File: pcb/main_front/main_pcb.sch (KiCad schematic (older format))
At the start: 31 parts, among them J1 AVR-ISP-6, J2 USB_C_Receptacle_USB2.0, Q1 Q_NMOS_DGS, SW1 RESET, SW2 BOOT, SW3 BL_STEP, U1 ATmega32-16PU, Y1 Crystal

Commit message: Begin revised PCB layout
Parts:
- removed D2: NUMLOCK, LED_THT:LED_D3.0mm_Clear, symbol Device:LED
- removed R9: 1.5k, Resistor_THT:R_Axial_DIN0204_L3.6mm_D1.6mm_P7.62mm_Horizontal, symbol Device:R
- added J3: Conn_01x16_Male, Connector_PinHeader_2.54mm:PinHeader_2x08_P2.54mm_Horizontal, symbol Connector:Conn_01x16_Male
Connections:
- net +5V: now also J3.16 (Pin_16)
- net GND: now also J3.15 (Pin_15)
- net LEDGND: now also J3.10 (Pin_10)
- net NUMLOCK: now also J3.11 (Pin_11)
- net col16: now also J3.9 (Pin_9)
- net col17: now also J3.8 (Pin_8)
- net col18: now also J3.7 (Pin_7)
- net col19: now also J3.6 (Pin_6)
- net row0: now also J3.5 (Pin_5)
- net row1: now also J3.4 (Pin_4)
- net row2: now also J3.3 (Pin_3)
- net row3: now also J3.2 (Pin_2)
- net row4: now also J3.1 (Pin_1)
- no-connect marks 3 -> 6
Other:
- moved on the sheet: D5, R10
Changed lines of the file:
@@
 encoding utf-8
 Sheet 1 2
-Title "QBoard - Front"
+Title "QBoard - Main"
 Date "2021-08-26"
 Rev "0"
@@
 L Device:LED D5
 U 1 1 6129195C
-P 7975 4350
-F 0 "D5" H 7968 4095 50  0000 C CNN
-F 1 "POWER" H 7968 4186 50  0000 C CNN
-F 2 "LED_THT:LED_D3.0mm_Clear" H 7975 4350 50  0001 C CNN
-F 3 "~" H 7975 4350 50  0001 C CNN
-	1    7975 4350
+P 7975 3825
+F 0 "D5" H 7968 3570 50  0000 C CNN
+F 1 "POWER" H 7968 3661 50  0000 C CNN
+F 2 "LED_THT:LED_D3.0mm_Clear" H 7975 3825 50  0001 C CNN
+F 3 "~" H 7975 3825 50  0001 C CNN
+	1    7975 3825
 	-1   0    0    1
 $EndComp
@@
 L Device:R R10
 U 1 1 612935EF
-P 8275 4350
-F 0 "R10" V 8175 4350 50  0000 C CNN
-F 1 "1.5k" V 8275 4350 50  0000 C CNN
-F 2 "Resistor_THT:R_Axial_DIN0204_L3.6mm_D1.6mm_P7.62mm_Horizontal" V 8205 4350 50  0001 C CNN
-F 3 "~" H 8275 4350 50  0001 C CNN
-	1    8275 4350
+P 8275 3825
+F 0 "R10" V 8175 3825 50  0000 C CNN
+F 1 "1.5k" V 8275 3825 50  0000 C CNN
+F 2 "Resistor_THT:R_Axial_DIN0204_L3.6mm_D1.6mm_P7.62mm_Horizontal" V 8205 3825 50  0001 C CNN
+F 3 "~" H 8275 3825 50  0001 C CNN
+	1    8275 3825
 	0    1    1    0
 $EndComp
@@
 L power:GND #PWR014
 U 1 1 612967E1
-P 8475 4350
-F 0 "#PWR014" H 8475 4100 50  0001 C CNN
-F 1 "GND" H 8480 4177 50  0000 C CNN
-F 2 "" H 8475 4350 50  0001 C CNN
-F 3 "" H 8475 4350 50  0001 C CNN
-	1    8475 4350
+P 8475 3825
+F 0 "#PWR014" H 8475 3575 50  0001 C CNN
+F 1 "GND" H 8480 3652 50  0000 C CNN
+F 2 "" H 8475 3825 50  0001 C CNN
+F 3 "" H 8475 3825 50  0001 C CNN
+	1    8475 3825
 	1    0    0    -1
 $EndComp
@@
 	8425 3400 8475 3400
 Wire Wire Line
-	8425 4350 8475 4350
+	8425 3825 8475 3825
 $Comp
 L power:+5V #PWR013
 U 1 1 612977F5
-P 7725 4350
-F 0 "#PWR013" H 7725 4200 50  0001 C CNN
-F 1 "+5V" H 7740 4523 50  0000 C CNN
-F 2 "" H 7725 4350 50  0001 C CNN
-F 3 "" H 7725 4350 50  0001 C CNN
-	1    7725 4350
-	1    0    0    -1
-$EndComp
-Wire Wire Line
-	7725 4350 7825 4350
+P 7725 3825
+F 0 "#PWR013" H 7725 3675 50  0001 C CNN
+F 1 "+5V" H 7740 3998 50  0000 C CNN
+F 2 "" H 7725 3825 50  0001 C CNN
+F 3 "" H 7725 3825 50  0001 C CNN
+	1    7725 3825
+	1    0    0    -1
+$EndComp
+Wire Wire Line
+	7725 3825 7825 3825
 $Comp
 L Connector:AVR-ISP-6 J1
@@
 Wire Wire Line
 	9475 4700 9600 4700
-Text GLabel 9600 4900 0    50   Input ~ 0
+Text GLabel 9600 5100 0    50   Input ~ 0
 row0
-Text GLabel 9600 5000 0    50   Input ~ 0
+Text GLabel 9600 5200 0    50   Input ~ 0
 row1
-Text GLabel 9600 5100 0    50   Input ~ 0
+Text GLabel 9600 5300 0    50   Input ~ 0
 row2
-Text GLabel 9600 5200 0    50   Input ~ 0
+Text GLabel 9600 5400 0    50   Input ~ 0
 row3
-Text GLabel 9600 5300 0    50   Input ~ 0
+Text GLabel 9600 5500 0    50   Input ~ 0
 row4
-Text GLabel 9600 5400 0    50   Input ~ 0
+Text GLabel 9600 5600 0    50   Input ~ 0
 row5
 $Sheet
@@
 F2 "5V" I L 9600 4700 50
 F3 "LEDGND" I L 9600 4800 50
-F4 "col0" I L 9600 5500 50
-F5 "col1" I L 9600 5600 50
-F6 "col2" I L 9600 5700 50
-F7 "col3" I L 9600 5800 50
-F8 "col4" I L 9600 5900 50
-F9 "col5" I L 9600 6000 50
-F10 "row0" I L 9600 4900 50
-F11 "row1" I L 9600 5000 50
-F12 "row2" I L 9600 5100 50
-F13 "row3" I L 9600 5200 50
-F14 "row4" I L 9600 5300 50
-F15 "row5" I L 9600 5400 50
-F16 "col6" I R 10250 4700 50
-F17 "col7" I R 10250 4800 50
-F18 "col8" I R 10250 4900 50
-F19 "col9" I R 10250 5000 50
-F20 "col10" I R 10250 5100 50
-F21 "col11" I R 10250 5200 50
-F22 "col12" I R 10250 5300 50
-F23 "col13" I R 10250 5400 50
-F24 "col14" I R 10250 5500 50
-F25 "col15" I R 10250 5600 50
-F26 "col16" I R 10250 5700 50
-F27 "col17" I R 10250 5800 50
-F28 "col18" I R 10250 5900 50
-F29 "col19" I R 10250 6000 50
+F4 "col0" I L 9600 5700 50
+F5 "col1" I L 9600 5800 50
+F6 "col2" I L 9600 5900 50
+F7 "col3" I L 9600 6000 50
+F8 "col4" I R 10250 4900 50
+F9 "col5" I R 10250 5000 50
+F10 "row0" I L 9600 5100 50
+F11 "row1" I L 9600 5200 50
+F12 "row2" I L 9600 5300 50
+F13 "row3" I L 9600 5400 50
+F14 "row4" I L 9600 5500 50
+F15 "row5" I L 9600 5600 50
+F16 "col6" I R 10250 5100 50
+F17 "col7" I R 10250 5200 50
+F18 "col8" I R 10250 5300 50
+F19 "col9" I R 10250 5400 50
+F20 "col10" I R 10250 5500 50
+F21 "col11" I R 10250 5600 50
+F22 "col12" I R 10250 5700 50
+F23 "col13" I R 10250 5800 50
+F24 "col14" I R 10250 5900 50
+F25 "col15" I R 10250 6000 50
 $EndSheet
-Text GLabel 9600 5500 0    50   Input ~ 0
+Text GLabel 9600 5700 0    50   Input ~ 0
 col0
-Text GLabel 9600 5600 0    50   Input ~ 0
+Text GLabel 9600 5800 0    50   Input ~ 0
 col1
-Text GLabel 9600 5700 0    50   Input ~ 0
+Text GLabel 9600 5900 0    50   Input ~ 0
 col2
-Text GLabel 9600 5800 0    50   Input ~ 0
+Text GLabel 9600 6000 0    50   Input ~ 0
 col3
-Text GLabel 9600 5900 0    50   Input ~ 0
+Text GLabel 10250 4900 2    50   Input ~ 0
 col4
-Text GLabel 9600 6000 0    50   Input ~ 0
+Text GLabel 10250 5000 2    50   Input ~ 0
 col5
-Text GLabel 10250 4700 2    50   Input ~ 0
+Text GLabel 10250 5100 2    50   Input ~ 0
 col6
-Text GLabel 10250 4800 2    50   Input ~ 0
+Text GLabel 10250 5200 2    50   Input ~ 0
 col7
-Text GLabel 10250 4900 2    50   Input ~ 0
+Text GLabel 10250 5300 2    50   Input ~ 0
 col8
-Text GLabel 10250 5000 2    50   Input ~ 0
+Text GLabel 10250 5400 2    50   Input ~ 0
 col9
-Text GLabel 10250 5100 2    50   Input ~ 0
+Text GLabel 10250 5500 2    50   Input ~ 0
 col10
-Text GLabel 10250 5200 2    50   Input ~ 0
+Text GLabel 10250 5600 2    50   Input ~ 0
 col11
-Text GLabel 10250 5300 2    50   Input ~ 0
+Text GLabel 10250 5700 2    50   Input ~ 0
 col12
-Text GLabel 10250 5400 2    50   Input ~ 0
+Text GLabel 10250 5800 2    50   Input ~ 0
 col13
-Text GLabel 10250 5500 2    50   Input ~ 0
+Text GLabel 10250 5900 2    50   Input ~ 0
 col14
-Text GLabel 10250 5600 2    50   Input ~ 0
+Text GLabel 10250 6000 2    50   Input ~ 0
 col15
-Text GLabel 10250 5700 2    50   Input ~ 0
-col16
-Text GLabel 10250 5800 2    50   Input ~ 0
-col17
-Text GLabel 10250 5900 2    50   Input ~ 0
-col18
-Text GLabel 10250 6000 2    50   Input ~ 0
-col19
 Text GLabel 6025 3175 2    50   Input ~ 0
 col0
@@
 Text GLabel 6025 5675 2    50   Input ~ 0
 BOOT
-$Comp
-L Device:LED D2
-U 1 1 6132A809
-P 7975 3875
-F 0 "D2" H 7968 3620 50  0000 C CNN
-F 1 "NUMLOCK" H 7968 3711 50  0000 C CNN
-F 2 "LED_THT:LED_D3.0mm_Clear" H 7975 3875 50  0001 C CNN
-F 3 "~" H 7975 3875 50  0001 C CNN
-	1    7975 3875
-	-1   0    0    1
-$EndComp
-$Comp
-L Device:R R9
-U 1 1 6132A80F
-P 8275 3875
-F 0 "R9" V 8175 3875 50  0000 C CNN
-F 1 "1.5k" V 8275 3875 50  0000 C CNN
-F 2 "Resistor_THT:R_Axial_DIN0204_L3.6mm_D1.6mm_P7.62mm_Horizontal" V 8205 3875 50  0001 C CNN
-F 3 "~" H 8275 3875 50  0001 C CNN
-	1    8275 3875
-	0    1    1    0
-$EndComp
-$Comp
-L power:GND #PWR010
-U 1 1 6132A815
-P 8475 3875
-F 0 "#PWR010" H 8475 3625 50  0001 C CNN
-F 1 "GND" H 8480 3702 50  0000 C CNN
-F 2 "" H 8475 3875 50  0001 C CNN
-F 3 "" H 8475 3875 50  0001 C CNN
-	1    8475 3875
-	1    0    0    -1
-$EndComp
-Wire Wire Line
-	8425 3875 8475 3875
-Text GLabel 7825 3875 0    50   Input ~ 0
+Text GLabel 9900 1275 0    50   Input ~ 0
 NUMLOCK
 $Comp
@@
 NoConn ~ 2375 4200
 NoConn ~ 2375 4300
+$Comp
+L Connector:Conn_01x16_Male J3
+U 1 1 61297A0F
+P 10100 1575
+F 0 "J3" H 10072 1457 50  0000 R CNN
+F 1 "Conn_01x16_Male" H 10072 1548 50  0000 R CNN
+F 2 "Connector_PinHeader_2.54mm:PinHeader_2x08_P2.54mm_Horizontal" H 10100 1575 50  0001 C CNN
+F 3 "~" H 10100 1575 50  0001 C CNN
+	1    10100 1575
+	-1   0    0    1
+$EndComp
+$Comp
+L power:+5V #PWR021
+U 1 1 614EDA42
+P 9800 775
+F 0 "#PWR021" H 9800 625 50  0001 C CNN
+F 1 "+5V" H 9650 825 50  0000 C CNN
+F 2 "" H 9800 775 50  0001 C CNN
+F 3 "" H 9800 775 50  0001 C CNN
+	1    9800 775
+	1    0    0    -1
+$EndComp
+Wire Wire Line
+	9800 775  9900 775
+$Comp
+L power:GND #PWR022
+U 1 1 614EF506
+P 9800 875
+F 0 "#PWR022" H 9800 625 50  0001 C CNN
+F 1 "GND" H 9650 825 50  0000 C CNN
+F 2 "" H 9800 875 50  0001 C CNN
+F 3 "" H 9800 875 50  0001 C CNN
+	1    9800 875
+	1    0    0    -1
+$EndComp
+Wire Wire Line
+	9800 875  9900 875
+NoConn ~ 9900 975
+NoConn ~ 9900 1075
+NoConn ~ 9900 1175
+Text GLabel 9900 1375 0    50   Input ~ 0
+LEDGND
+Text GLabel 9900 1475 0    50   Input ~ 0
+col16
+Text GLabel 9900 1575 0    50   Input ~ 0
+col17
+Text GLabel 9900 1675 0    50   Input ~ 0
+col18
+Text GLabel 9900 1775 0    50   Input ~ 0
+col19
+Text GLabel 9900 1875 0    50   Input ~ 0
+row0
+Text GLabel 9900 1975 0    50   Input ~ 0
+row1
+Text GLabel 9900 2075 0    50   Input ~ 0
+row2
+Text GLabel 9900 2175 0    50   Input ~ 0
+row3
+Text GLabel 9900 2275 0    50   Input ~ 0
+row4
 $EndSCHEMATC

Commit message: Fix wrong pinout on MOSFET
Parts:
- removed Q1: Q_NMOS_DGS, Package_TO_SOT_THT:TO-262-3_Vertical, symbol Device:Q_NMOS_DGS
- added Q1: Q_NMOS_GDS, Package_TO_SOT_THT:TO-262-3_Vertical, symbol Device:Q_NMOS_GDS
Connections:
- net GND: now also Q1.3 (S)
- net LEDGND: now also Q1.2 (D)
- net at R1.1, R2.1: now also Q1.1 (G)
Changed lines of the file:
@@
-$EndComp
-$Comp
-L Device:Q_NMOS_DGS Q1
-U 1 1 6130149A
-P 8000 2400
-F 0 "Q1" H 8204 2446 50  0000 L CNN
-F 1 "Q_NMOS_DGS" H 8204 2355 50  0000 L CNN
-F 2 "Package_TO_SOT_THT:TO-262-3_Vertical" H 8200 2500 50  0001 C CNN
-F 3 "~" H 8000 2400 50  0001 C CNN
-	1    8000 2400
-	1    0    0    -1
 $EndComp
 $Comp
@@
 Text GLabel 9900 2275 0    50   Input ~ 0
 row4
+$Comp
+L Device:Q_NMOS_GDS Q1
+U 1 1 61352FA9
+P 8000 2400
+F 0 "Q1" H 8204 2446 50  0000 L CNN
+F 1 "Q_NMOS_GDS" H 8204 2355 50  0000 L CNN
+F 2 "Package_TO_SOT_THT:TO-262-3_Vertical" H 8200 2500 50  0001 C CNN
+F 3 "~" H 8000 2400 50  0001 C CNN
+	1    8000 2400
+	1    0    0    -1
+$EndComp
 $EndSCHEMATC

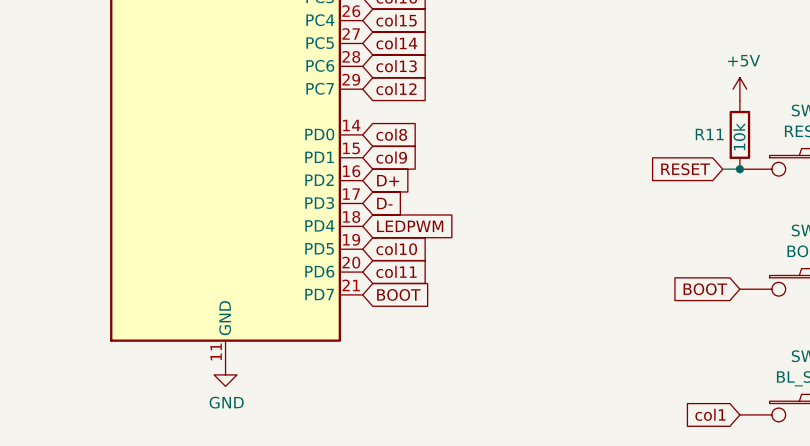
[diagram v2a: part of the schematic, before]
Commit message: Fix pin issue in schematic and netlist
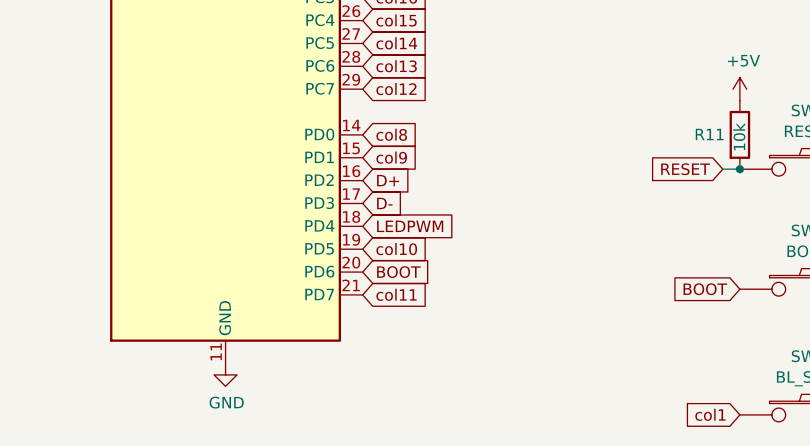
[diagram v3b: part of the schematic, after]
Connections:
- net BOOT: now also U1.20 (PD6); no longer U1.21 (PD7)
- net col11: now also U1.21 (PD7); no longer U1.20 (PD6)
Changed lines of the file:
@@
 Text GLabel 6025 4775 2    50   Input ~ 0
 col12
-Text GLabel 6025 5575 2    50   Input ~ 0
+Text GLabel 6025 5675 2    50   Input ~ 0
 col11
 Text GLabel 7675 5650 0    50   Input ~ 0
 BOOT
-Text GLabel 6025 5675 2    50   Input ~ 0
+Text GLabel 6025 5575 2    50   Input ~ 0
 BOOT
 Text GLabel 9900 1275 0    50   Input ~ 0
